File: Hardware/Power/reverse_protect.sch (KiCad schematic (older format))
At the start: 3 parts, among them Q5 SUD08P06-155L

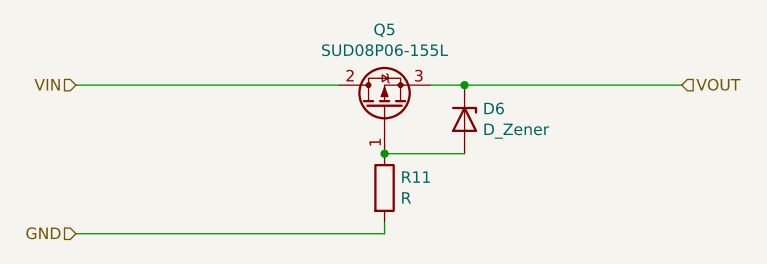
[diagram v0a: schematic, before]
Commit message: Removed Logic Board PSU from Power Board
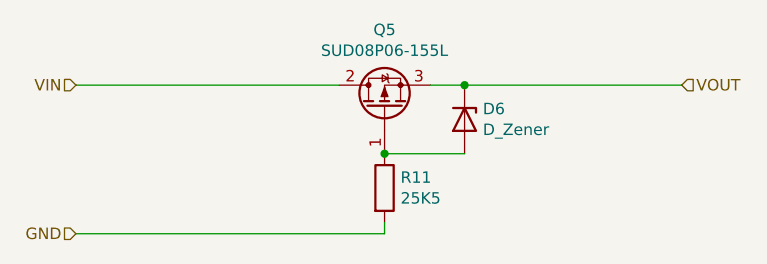
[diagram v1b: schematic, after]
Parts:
- R11: value R -> 25K5
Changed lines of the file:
@@
 P 5350 3450
 F 0 "R11" H 5420 3496 50  0000 L CNN
-F 1 "R" H 5420 3405 50  0000 L CNN
+F 1 "25K5" H 5420 3405 50  0000 L CNN
 F 2 "Resistor_SMD:R_0603_1608Metric_Pad1.05x0.95mm_HandSolder" V 5280 3450 50  0001 C CNN
 F 3 "~" H 5350 3450 50  0001 C CNN
